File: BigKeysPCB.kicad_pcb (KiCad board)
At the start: 2 copper layers, 100 x 100 mm, 24 parts, among them SW1 SW_Push, U1 ATmega32U4-M, Y1 16MHz

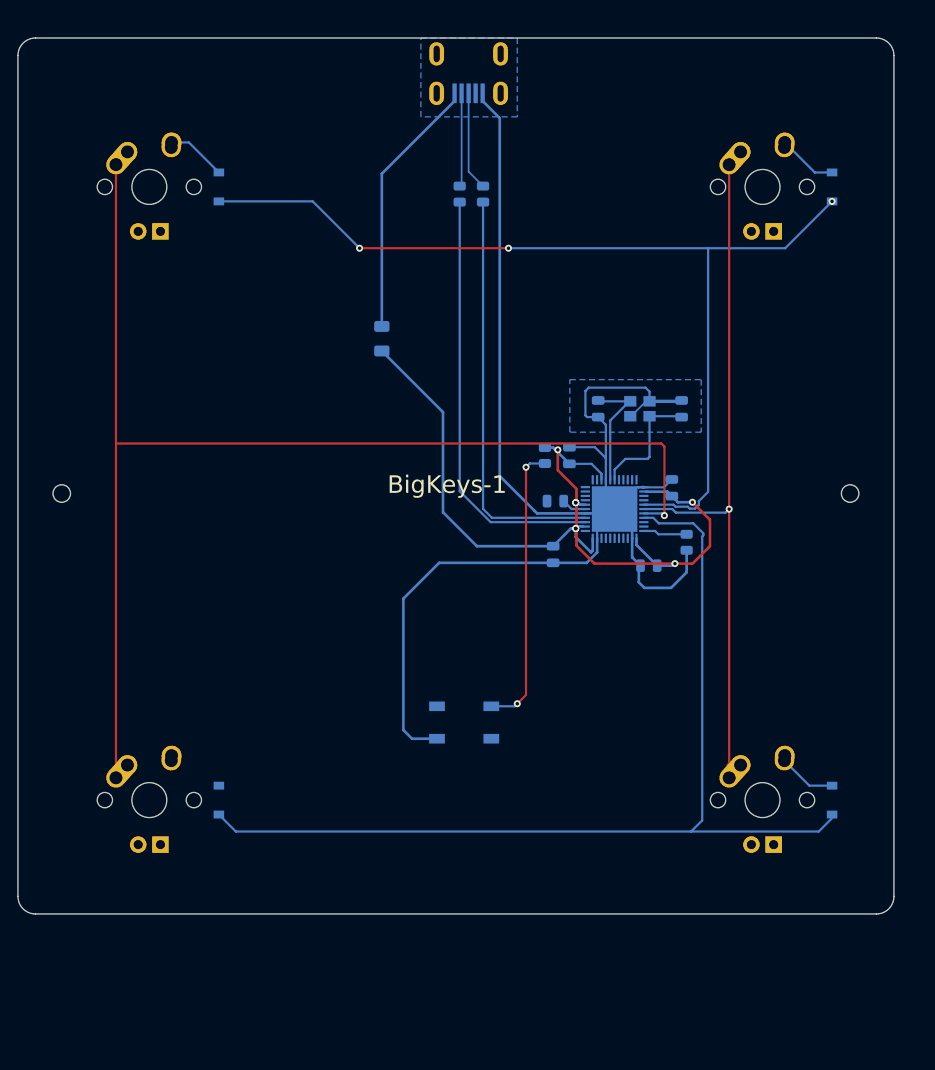
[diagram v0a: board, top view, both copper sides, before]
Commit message: changed wiring, some errors and warnings solved
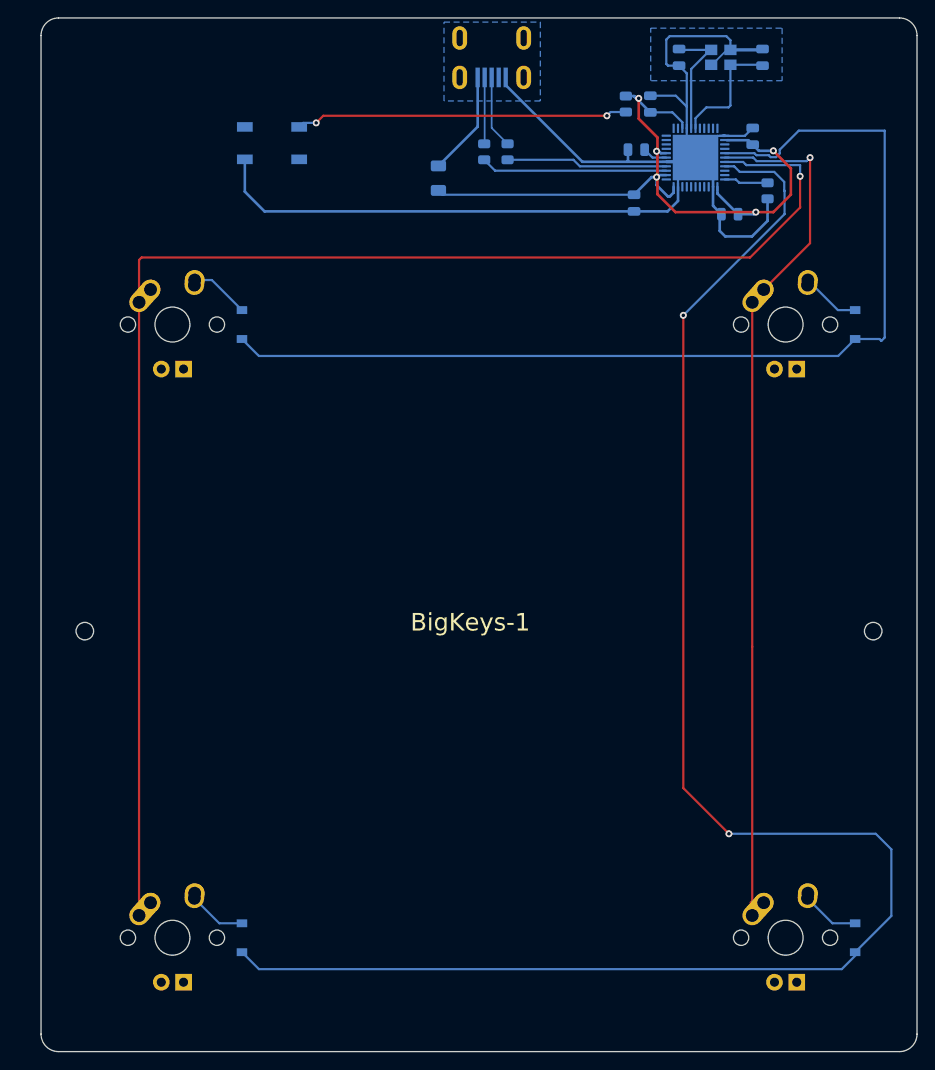
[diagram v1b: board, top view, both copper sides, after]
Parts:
- moved SW1 69.7 mm to (117.0, 54.0)
- moved C1 41.2 mm to (173.0, 44.2)
- moved C2 41.2 mm to (163.5, 44.2)
- moved C4 41.2 mm to (160.2, 49.5)
- moved R1 41.2 mm to (157.4, 49.5)
- moved Y1 41.2 mm to (168.2, 44.2)
- moved C3 41.2 mm to (158.6, 54.7)
- moved C5 41.2 mm to (171.9, 53.2)
- moved C6 41.2 mm to (169.3, 62.1)
- moved R4 41.2 mm to (173.6, 59.4)
- moved U1 41.2 mm to (165.3, 55.6)
- moved C7 41.2 mm to (158.3, 60.8)
- moved F1 19.4 mm to (136.0, 58.0)
- moved D2 15.9 mm to (113.6, 144.7)
- moved D4 15.9 mm to (183.6, 144.7)
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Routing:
- net ROW1: track 113.7 -> 193.2 mm, vias 0 -> 2
- net Net-(R2-Pad2): track 47.1 -> 18.4 mm
- net Net-(R3-Pad2): track 48.8 -> 21.3 mm
- net COL0: track 141.3 -> 164.7 mm
- net VCC: track 30.1 -> 12.0 mm
- net GND: track 165.9 -> 148.7 mm
- net COL1: track 78.7 -> 95.9 mm
- net +5V: track 102.3 -> 88.6 mm, vias 7 -> 5
- net ROW0: track 110.8 -> 118.8 mm, vias 3 -> 0
- net Net-(D2-Pad2): track 0.00 -> 6.62 mm
- net Net-(R1-Pad2): track 32.8 -> 38.0 mm
- net D+: track 11.3 -> 8.33 mm
- net D-: track 10.7 -> 7.91 mm
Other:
- board size 100 x 100 mm -> 100 x 118 mm

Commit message: correct measures for 3D case and plate model
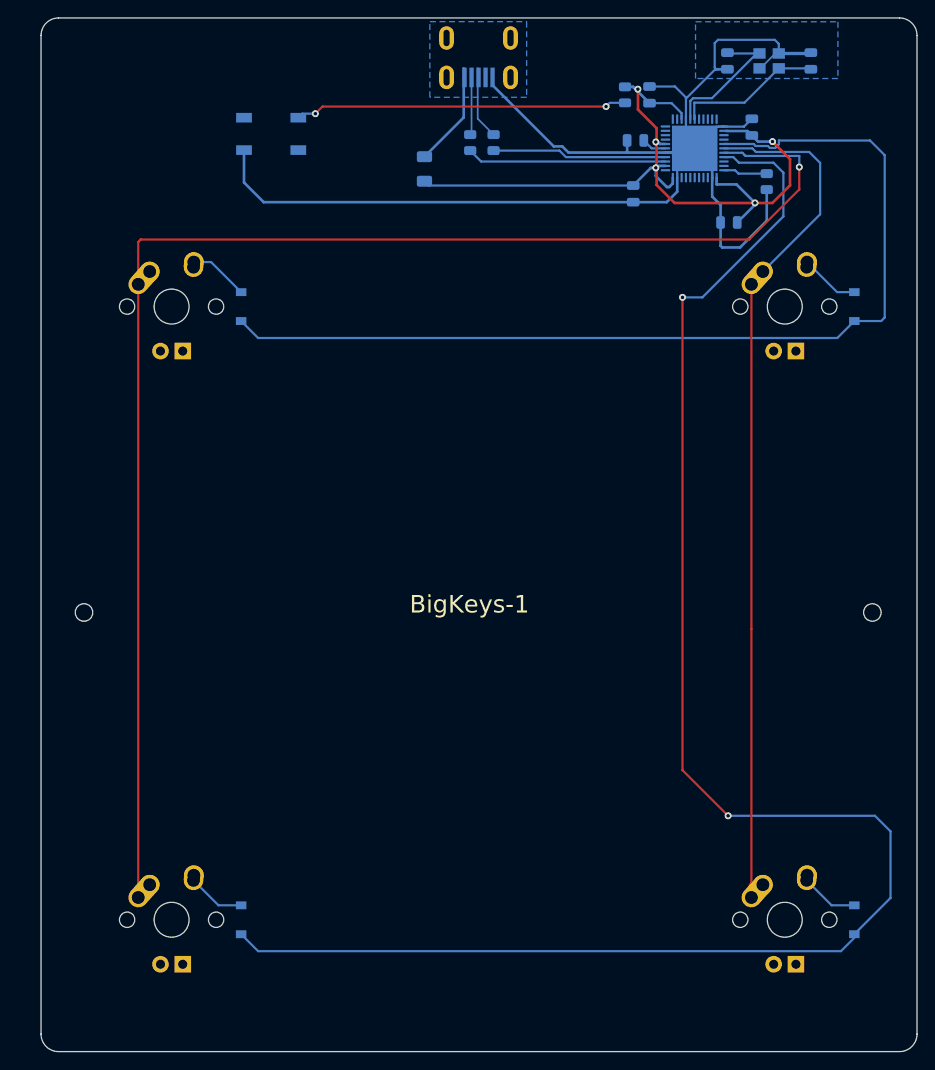
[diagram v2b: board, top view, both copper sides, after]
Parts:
- moved C1 5.54 mm to (178.5, 44.6)
- moved Y1 5.54 mm to (173.8, 44.6)
- moved C2 5.54 mm to (169.0, 44.6)
- moved D4 2.05 mm to (183.5, 142.7)
- moved MX4 2.05 mm to (175.5, 142.7)
- moved D2 2.05 mm to (113.5, 142.7)
- moved MX2 2.05 mm to (105.5, 142.7)
- moved D3 2.05 mm to (183.5, 72.7)
- moved MX3 2.05 mm to (175.5, 72.7)
- moved D1 2.05 mm to (113.5, 72.7)
- moved MX1 2.05 mm to (105.5, 72.7)
- moved F1 1.91 mm to (134.4, 56.9)
- moved R2 1.91 mm to (142.3, 53.9)
- moved R3 1.91 mm to (139.6, 53.9)
- moved USB1 1.50 mm to (140.6, 42.0)
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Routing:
- net GND: track 148.7 -> 154.6 mm
- net ROW0: track 118.8 -> 113.6 mm
- net +5V: track 88.6 -> 93.0 mm
- net Net-(C1-Pad2): track 14.1 -> 16.9 mm
- net Net-(C2-Pad2): track 13.7 -> 15.9 mm
- net Net-(R3-Pad2): track 21.3 -> 22.8 mm
- net Net-(R2-Pad2): track 18.4 -> 19.9 mm
- net D-: track 7.91 -> 6.89 mm
- net COL0: track 164.7 -> 163.7 mm
- net COL1: track 95.9 -> 95.4 mm, vias 1 -> 0
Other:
- outline, holes or cut-outs redrawn

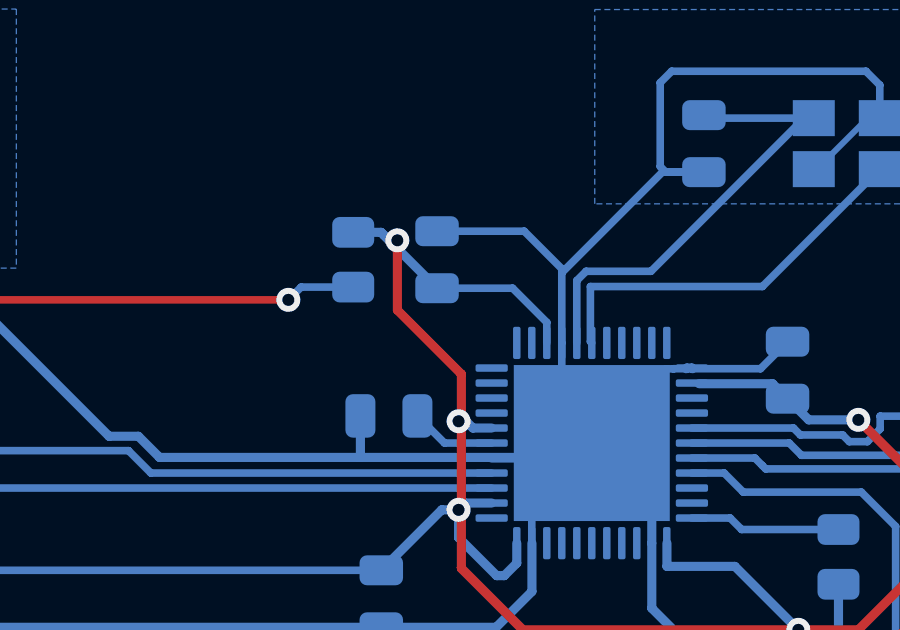
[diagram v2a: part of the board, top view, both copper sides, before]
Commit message: shield connected to ground, missing connection added to pcb file
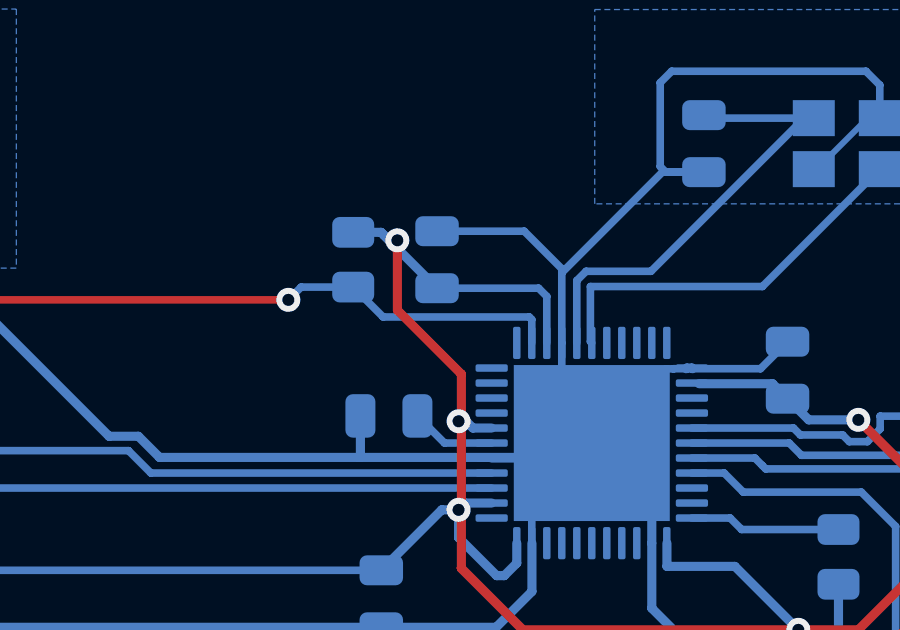
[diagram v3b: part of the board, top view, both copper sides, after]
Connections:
- USB1 pad 6: unconnected-(USB1-Pad6) -> GND
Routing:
- net Net-(R1-Pad2): track 38.0 -> 45.2 mm
- net +5V: track 93.0 -> 93.5 mm
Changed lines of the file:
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@@
   (net 42 "unconnected-(U1-Pad42)")
   (net 43 "unconnected-(USB1-Pad2)")
-  (net 44 "unconnected-(USB1-Pad6)")
   (footprint "MX_Alps_Hybrid:MX-1U" (layer "F.Cu")
     (at 175.54 142.66)
@@
       (net 12 "VCC") (pinfunction "VBUS") (pintype "input"))
     (pad "6" thru_hole oval locked (at 0 3.65 270) (size 2.7 1.7) (drill oval 1.9 0.7) (layers *.Cu *.Mask)
-      (net 44 "unconnected-(USB1-Pad6)") (pinfunction "SHIELD") (pintype "input"))
+      (net 4 "GND") (pinfunction "SHIELD") (pintype "input"))
     (pad "6" thru_hole oval locked (at 0 -3.65 270) (size 2.7 1.7) (drill oval 1.9 0.7) (layers *.Cu *.Mask)
-      (net 44 "unconnected-(USB1-Pad6)") (pinfunction "SHIELD") (pintype "input"))
+      (net 4 "GND") (pinfunction "SHIELD") (pintype "input"))
     (pad "6" thru_hole oval locked (at 4.5 3.65 270) (size 2.7 1.7) (drill oval 1.9 0.7) (layers *.Cu *.Mask)
-      (net 44 "unconnected-(USB1-Pad6)") (pinfunction "SHIELD") (pintype "input"))
+      (net 4 "GND") (pinfunction "SHIELD") (pintype "input"))
     (pad "6" thru_hole oval locked (at 4.5 -3.65 270) (size 2.7 1.7) (drill oval 1.9 0.7) (layers *.Cu *.Mask)
-      (net 44 "unconnected-(USB1-Pad6)") (pinfunction "SHIELD") (pintype "input"))
+      (net 4 "GND") (pinfunction "SHIELD") (pintype "input"))
   )
   (footprint "Diode_SMD:D_SOD-123" (layer "B.Cu")
@@
   (segment (start 158.313 47.653481) (end 160.097 49.437481) (width 0.3048) (layer "B.Cu") (net 5))
   (segment (start 158.2345 47.574981) (end 158.313 47.653481) (width 0.3048) (layer "B.Cu") (net 5))
-  (segment (start 162.618 49.437481) (end 163.7555 50.574981) (width 0.254) (layer "B.Cu") (net 5))
   (segment (start 158.313 47.653481) (end 158.500481 47.840962) (width 0.3048) (layer "B.Cu") (net 5))
-  (segment (start 160.097 49.437481) (end 162.618 49.437481) (width 0.254) (layer "B.Cu") (net 5))
   (segment (start 162.7555 57.935981) (end 162.7555 58.602481) (width 0.3048) (layer "B.Cu") (net 5))
   (segment (start 171.2816 52.621081) (end 168.829496 52.621081) (width 0.3048) (layer "B.Cu") (net 5))
@@
   (segment (start 162.7555 58.602481) (end 162.3385 59.019481) (width 0.3048) (layer "B.Cu") (net 5))
   (segment (start 162.3385 59.019481) (end 162.0845 59.019481) (width 0.3048) (layer "B.Cu") (net 5))
-  (segment (start 163.7555 50.574981) (end 163.7555 51.260981) (width 0.254) (layer "B.Cu") (net 5))
+  (segment (start 163.483481 49.437481) (end 163.7555 49.7095) (width 0.254) (layer "B.Cu") (net 5))
   (segment (start 161.067243 53.871981) (end 161.293743 54.098481) (width 0.3048) (layer "B.Cu") (net 5))
   (segment (start 158.239 58.840481) (end 134.8975 58.840481) (width 0.254) (layer "B.Cu") (net 5))
@@
   (segment (start 158.239 58.840481) (end 158.559 58.840481) (width 0.254) (layer "B.Cu") (net 5))
   (segment (start 157.303 47.574981) (end 158.2345 47.574981) (width 0.3048) (layer "B.Cu") (net 5))
+  (segment (start 160.097 49.437481) (end 163.483481 49.437481) (width 0.254) (layer "B.Cu") (net 5))
+  (segment (start 163.7555 49.7095) (end 163.7555 51.260981) (width 0.254) (layer "B.Cu") (net 5))
   (segment (start 160.815526 57.750507) (end 160.815526 56.824981) (width 0.3048) (layer "B.Cu") (net 5))
   (segment (start 171.781 53.120481) (end 171.2816 52.621081) (width 0.3048) (layer "B.Cu") (net 5))
@@
   (via (at 155.141 49.825481) (size 0.8) (drill 0.4) (layers "F.Cu" "B.Cu") (net 15))
   (segment (start 120.4665 50.637481) (end 120.0055 51.098481) (width 0.254) (layer "B.Cu") (net 15))
+  (segment (start 163.2555 50.4795) (end 163.2555 51.260981) (width 0.254) (layer "B.Cu") (net 15))
   (segment (start 155.5665 49.399981) (end 155.141 49.825481) (width 0.254) (layer "B.Cu") (net 15))
+  (segment (start 163.172481 50.396481) (end 163.2555 50.4795) (width 0.254) (layer "B.Cu") (net 15))
   (segment (start 157.303 49.399981) (end 155.5665 49.399981) (width 0.254) (layer "B.Cu") (net 15))
   (segment (start 121.9525 50.637481) (end 120.4665 50.637481) (width 0.254) (layer "B.Cu") (net 15))
+  (segment (start 158.2995 50.396481) (end 163.172481 50.396481) (width 0.254) (layer "B.Cu") (net 15))
+  (segment (start 157.303 49.399981) (end 158.2995 50.396481) (width 0.254) (layer "B.Cu") (net 15))
   (segment (start 140.486 45.448481) (end 140.486 51.216481) (width 0.2) (layer "B.Cu") (net 16))
   (segment (start 140.486 51.216481) (end 142.2965 53.026981) (width 0.2) (layer "B.Cu") (net 16))
